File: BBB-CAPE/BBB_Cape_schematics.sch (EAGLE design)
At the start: 84 parts, among them IC1 EEPROM-I2CSMD, SW2 219-02

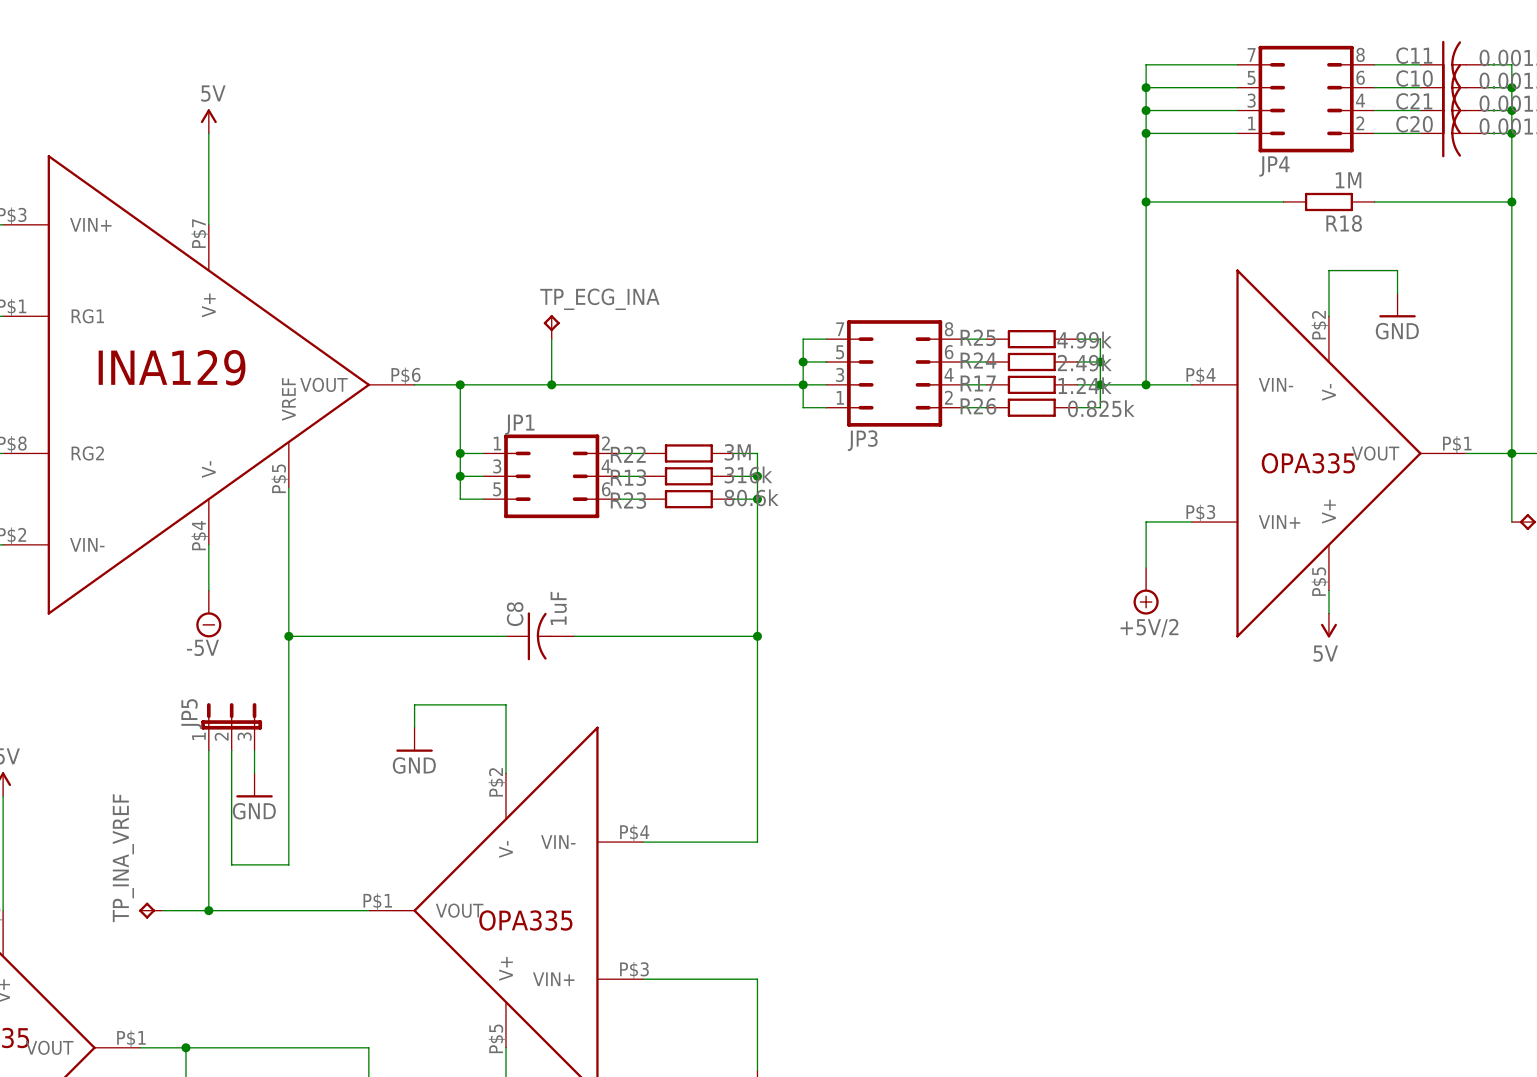
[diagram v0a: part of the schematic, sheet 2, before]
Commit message: Add pin no 1 mark on SOIC-8 and SSOP-8 package in Components.lbr Replace Jumper by Solder jump in BBB_Cape_schematics.sch
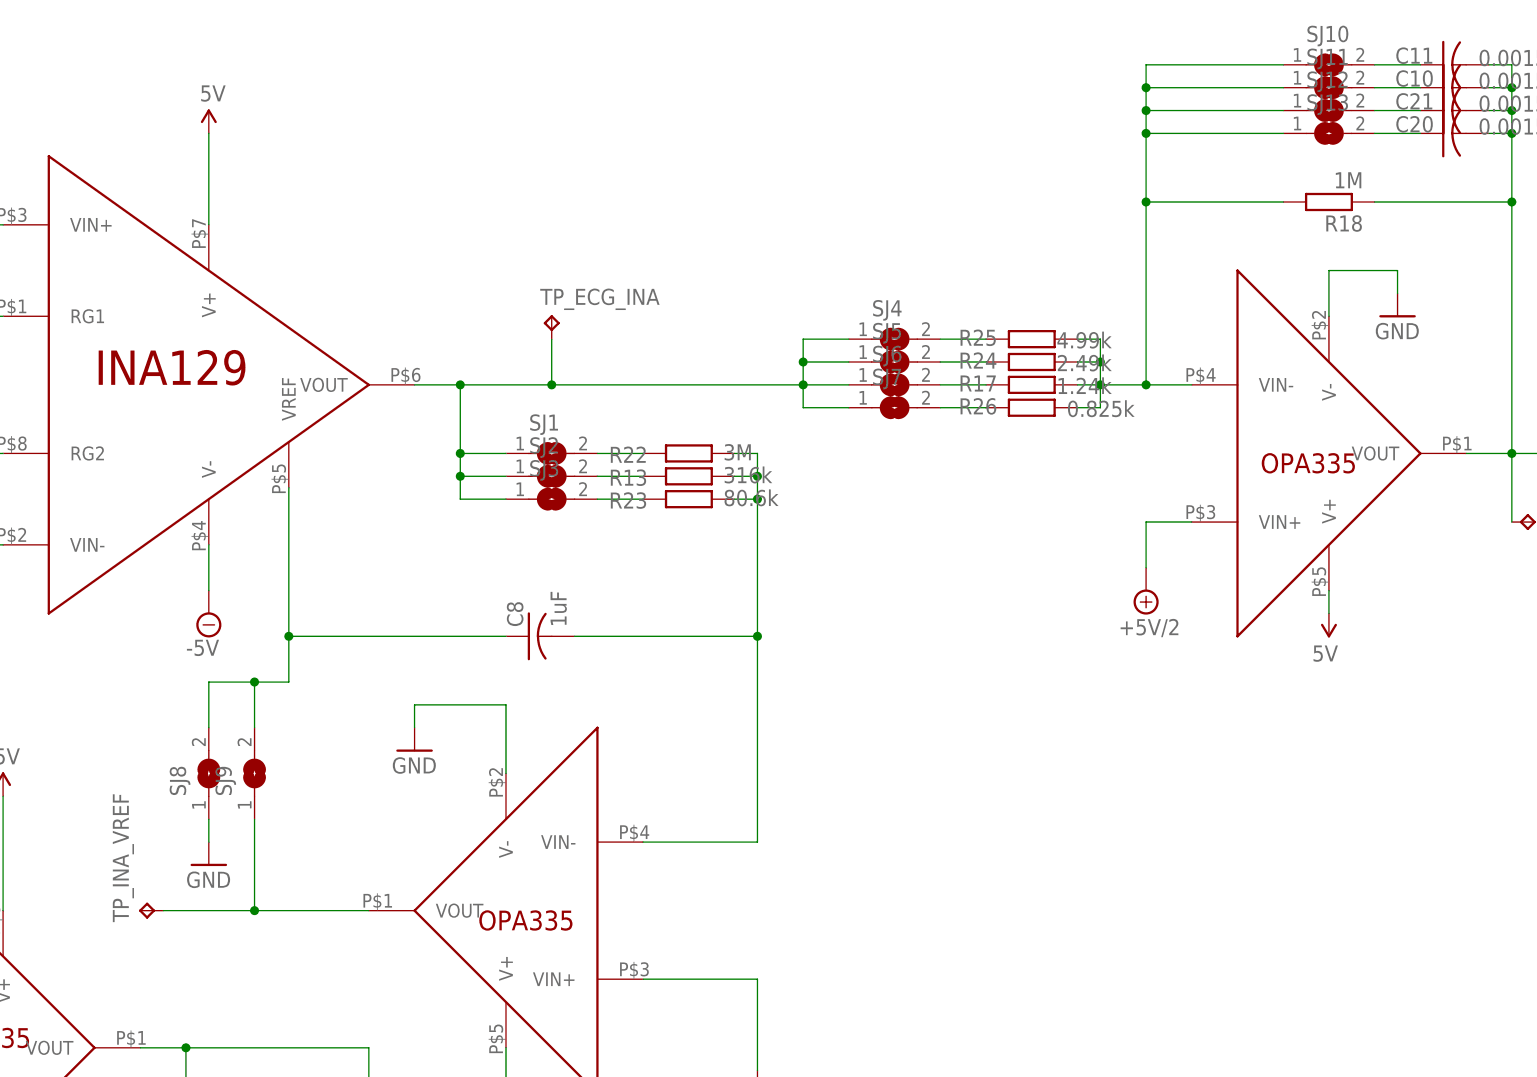
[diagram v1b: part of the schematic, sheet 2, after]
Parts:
- removed JP1: (no value), jumper:JP3Q
- removed JP3, JP4: (no value), jumper:JP4Q
- removed JP5: (no value), jumper:JP2E
- added SJ1, SJ10, SJ11, SJ12, SJ13, SJ2, SJ3, SJ4, SJ5, SJ6, SJ7, SJ8, SJ9: (no value), jumper:SJW
- added TP3, TP4, TP5: TPB2,54, testpad:TPB2,54
- BB1: value BBH2 -> BBH1; device logic-supply:BBH2 -> logic-supply:BBH1
- renumbered U$5 to U5
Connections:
- removed net N$44: C20.1, JP4.2
- new net N$36: R25.2, SJ4.2
- net ADC_DOUT: now also TP3.TP
- net ADC_SCLK: now also TP4.TP
- net GND: now also SJ8.1; no longer JP5.3
- net N$10: now also SJ8.2, SJ9.2; no longer JP5.2
- net N$11: now also SJ1.1, SJ2.1, SJ3.1, SJ4.1, SJ5.1, SJ6.1, SJ7.1; no longer JP1.1, JP1.3, JP1.5, JP3.1, JP3.3, JP3.5, JP3.7
- net N$18: now also SJ10.1, SJ11.1, SJ12.1, SJ13.1; no longer JP4.1, JP4.3, JP4.5, JP4.7
- net N$29: now also TP5.TP
- net N$32: now also SJ1.2; no longer JP1.2
- net N$33: now also SJ2.2; no longer JP1.4
- net N$34: now also SJ3.2; no longer JP1.6
- net N$35: now also SJ9.1; no longer JP5.1
- net N$37: now also R24.2, SJ5.2; no longer JP3.8, R25.2
- net N$38: now also R17.2, SJ6.2; no longer JP3.6, R24.2
- net N$39: now also R26.2, SJ7.2; no longer JP3.4, R17.2
- net N$40: now also C11.1, SJ10.2; no longer JP3.2, R26.2
- net N$41: now also C10.1, SJ11.2; no longer C11.1, JP4.8
- net N$42: now also C21.1, SJ12.2; no longer C10.1, JP4.6
- net N$43: now also C20.1, SJ13.2; no longer C21.1, JP4.4

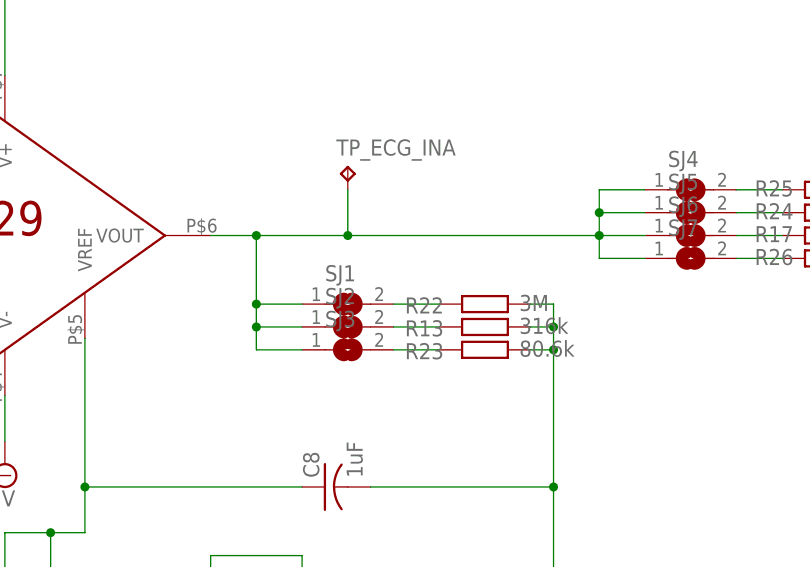
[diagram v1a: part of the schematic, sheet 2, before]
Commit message: Remove one Resistor from LPF in in BBB_Cape_schematics.sch
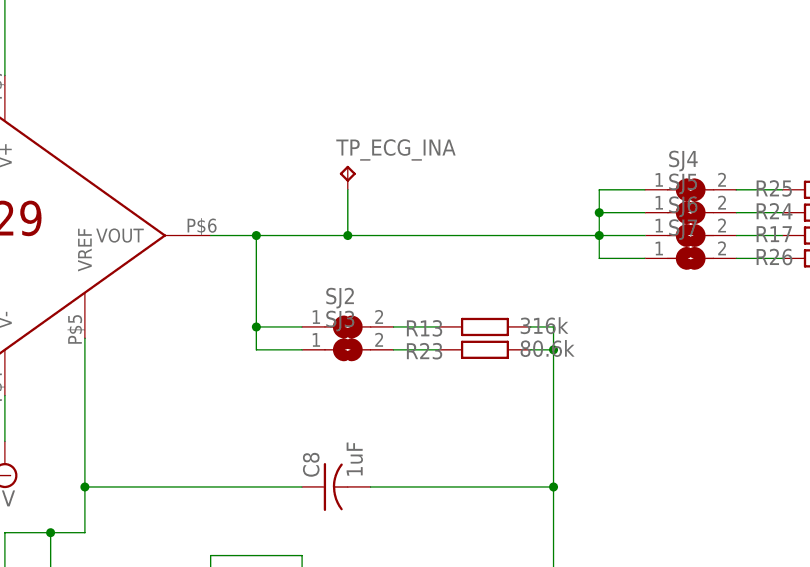
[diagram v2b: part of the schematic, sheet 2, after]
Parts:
- removed R22: 3M, resistor:R-EU_M1206
- removed SJ1: (no value), jumper:SJW
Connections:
- removed net N$32: R22.1, SJ1.2
- net N$11: no longer SJ1.1
- net N$12: no longer R22.2
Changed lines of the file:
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@@
 <part name="R21" library="resistor" deviceset="R-EU_" device="M1206" value="10k"/>
 <part name="P+13" library="SparkFun-Aesthetics" deviceset="3.3V" device=""/>
-<part name="R22" library="resistor" deviceset="R-EU_" device="M1206" value="3M"/>
 <part name="R23" library="resistor" deviceset="R-EU_" device="M1206" value="80.6k"/>
 <part name="GND27" library="supply1" deviceset="GND" device=""/>
@@
 <part name="TP4" library="testpad" deviceset="TP" device="B2,54"/>
 <part name="TP5" library="testpad" deviceset="TP" device="B2,54"/>
-<part name="SJ1" library="jumper" deviceset="SJ" device="W"/>
 <part name="SJ2" library="jumper" deviceset="SJ" device="W"/>
 <part name="SJ3" library="jumper" deviceset="SJ" device="W"/>
@@
 <instance part="TP_ECG_INA" gate="G$1" x="220.98" y="195.58"/>
 <instance part="TP_INA_VREF" gate="G$1" x="175.26" y="129.54" rot="R90"/>
-<instance part="R22" gate="G$1" x="236.22" y="180.34" smashed="yes">
-<attribute name="NAME" x="227.33" y="179.2986" size="1.778" layer="95"/>
-<attribute name="VALUE" x="240.03" y="179.578" size="1.778" layer="96"/>
-</instance>
 <instance part="R23" gate="G$1" x="236.22" y="175.26" smashed="yes">
 <attribute name="NAME" x="227.33" y="174.2186" size="1.778" layer="95"/>
@@
 <instance part="U$31" gate="G$1" x="182.88" y="215.9"/>
 <instance part="U$32" gate="G$1" x="307.34" y="162.56" rot="R180"/>
-<instance part="SJ1" gate="1" x="220.98" y="180.34"/>
 <instance part="SJ2" gate="1" x="220.98" y="177.8"/>
 <instance part="SJ3" gate="1" x="220.98" y="175.26"/>
@@
 <wire x1="210.82" y1="187.96" x2="220.98" y2="187.96" width="0.1524" layer="91"/>
 <wire x1="220.98" y1="193.04" x2="220.98" y2="187.96" width="0.1524" layer="91"/>
-<wire x1="210.82" y1="187.96" x2="210.82" y2="180.34" width="0.1524" layer="91"/>
+<wire x1="210.82" y1="187.96" x2="210.82" y2="177.8" width="0.1524" layer="91"/>
 <junction x="210.82" y="187.96"/>
 <pinref part="SJ3" gate="1" pin="1"/>
-<wire x1="210.82" y1="180.34" x2="210.82" y2="177.8" width="0.1524" layer="91"/>
 <wire x1="210.82" y1="177.8" x2="210.82" y2="175.26" width="0.1524" layer="91"/>
 <wire x1="210.82" y1="175.26" x2="215.9" y2="175.26" width="0.1524" layer="91"/>
@@
 <wire x1="215.9" y1="177.8" x2="210.82" y2="177.8" width="0.1524" layer="91"/>
 <junction x="210.82" y="177.8"/>
-<pinref part="SJ1" gate="1" pin="1"/>
-<wire x1="215.9" y1="180.34" x2="210.82" y2="180.34" width="0.1524" layer="91"/>
-<junction x="210.82" y="180.34"/>
 <wire x1="220.98" y1="187.96" x2="248.92" y2="187.96" width="0.1524" layer="91"/>
 <junction x="220.98" y="187.96"/>
@@
 <pinref part="U$9" gate="G$1" pin="VIN-"/>
 <wire x1="243.84" y1="137.16" x2="231.14" y2="137.16" width="0.1524" layer="91"/>
-<pinref part="R22" gate="G$1" pin="2"/>
-<wire x1="241.3" y1="180.34" x2="243.84" y2="180.34" width="0.1524" layer="91"/>
-<wire x1="243.84" y1="180.34" x2="243.84" y2="177.8" width="0.1524" layer="91"/>
 <junction x="243.84" y="160.02"/>
 <pinref part="R13" gate="G$1" pin="2"/>
@@
 <wire x1="243.84" y1="175.26" x2="243.84" y2="160.02" width="0.1524" layer="91"/>
 <wire x1="241.3" y1="177.8" x2="243.84" y2="177.8" width="0.1524" layer="91"/>
-<junction x="243.84" y="177.8"/>
 <pinref part="R23" gate="G$1" pin="2"/>
 <wire x1="241.3" y1="175.26" x2="243.84" y2="175.26" width="0.1524" layer="91"/>
@@
 </segment>
 </net>
-<net name="N$32" class="0">
-<segment>
-<pinref part="SJ1" gate="1" pin="2"/>
-<pinref part="R22" gate="G$1" pin="1"/>
-<wire x1="226.06" y1="180.34" x2="231.14" y2="180.34" width="0.1524" layer="91"/>
-</segment>
-</net>

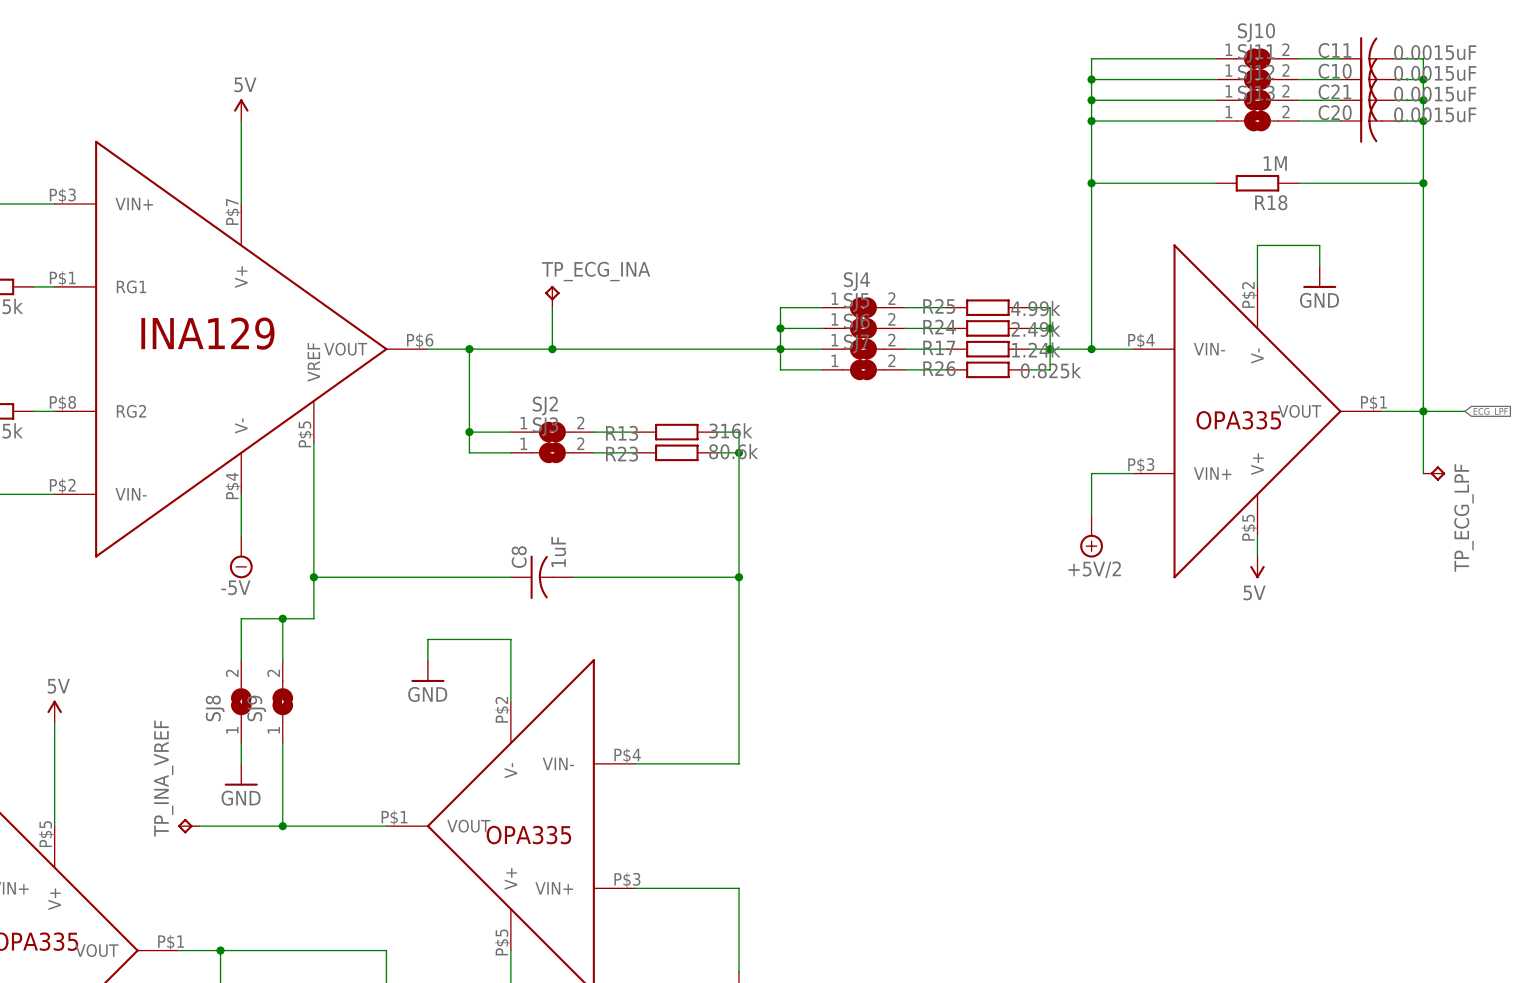
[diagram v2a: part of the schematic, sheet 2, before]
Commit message: Replace solder jump by 0.1 inch header to save space in board in BBB_Cape_schematics.sch
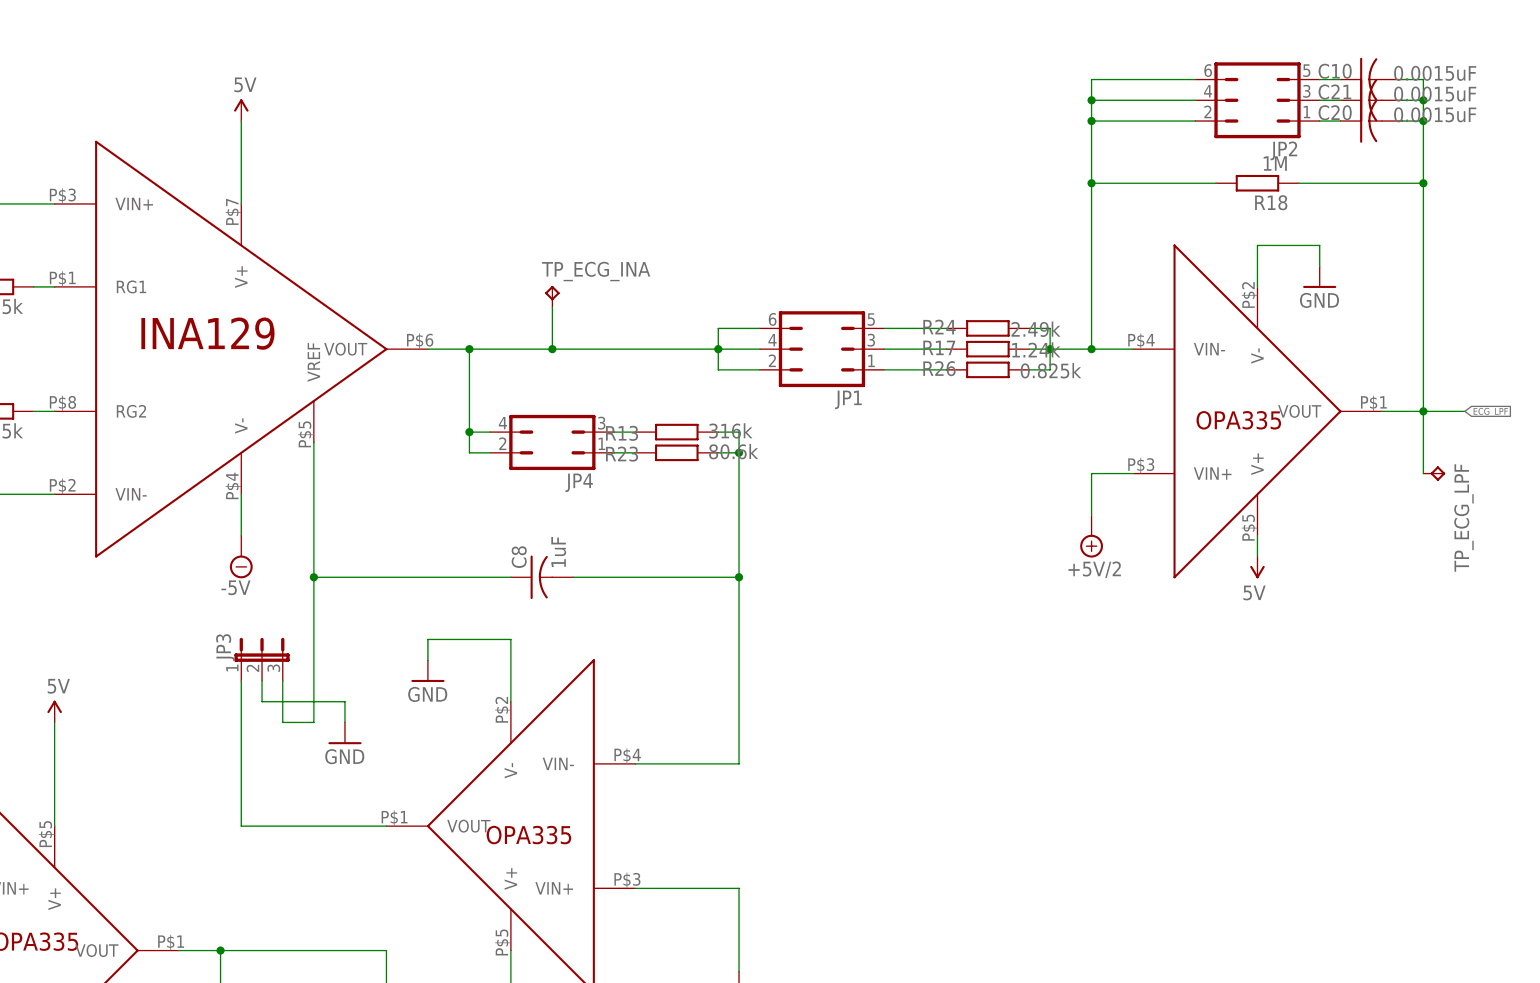
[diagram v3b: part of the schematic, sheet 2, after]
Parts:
- removed C1: 0.1uF, logic-supply:C0402
- removed C11: 0.0015uF, rcl:C-USC1206
- removed IC1: EEPROM-I2CSMD, logic-supply:EEPROM-I2CSMD
- removed R1, R2, R3, R4, R5, R6: 5.6k, logic-supply:R0402
- removed R25: 4.99k, resistor:R-EU_M1206
- removed S2, SW2: 219-02, switch-dil:219-02
- removed SJ10, SJ11, SJ12, SJ13, SJ2, SJ3, SJ4, SJ5, SJ6, SJ7, SJ8, SJ9: (no value), jumper:SJW
- removed TP1, TP2: TEST_POINT, logic-supply:TEST_POINT
- removed TP1_2.5V, TP_INA_VREF: TPB2,54, testpad:TPB2,54
- added JP1, JP2: (no value), jumper:JP3Q
- added JP3: (no value), jumper:JP2E
- added JP4, JP5: (no value), jumper:JP2Q
- renumbered U$10 to U10, U$11 to U11, U$12 to U12, U$13 to U13, U$14 to U14, U$16 to LH, U$17 to RH, U$18 to LH_INDEX, U$19 to U19, U$21 to U21, U$22 to U22, U$23 to U23, U$24 to RH_INDEX, U$4 to U4, U$9 to U9
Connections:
- removed net N$13: IC1.A0, R3.1, SW2.4
- removed net N$14: IC1.A1, R2.1, SW2.3
- removed net N$15: IC1.A2, R1.1
- removed net N$39: R26.2, SJ7.2
- removed net N$43: C20.1, SJ13.2
- removed net WP: IC1.WP, R4.1, TP2.P$1
- net 3.3V: now also JP5.2, JP5.4; no longer C1.1, IC1.VCC, R1.2, R2.2, R3.2, R4.2, R5.2, R6.2, S2.1, S2.2
- net ECG_LPF: no longer C11.2
- net GND: now also JP3.2; no longer C1.2, IC1.VSS, SJ8.1, SW2.1, SW2.2, TP1.P$1
- net I2C2_SCL: no longer IC1.SCL, R5.1
- net I2C2_SDA: no longer IC1.SDA, R6.1
- net N$10: now also JP3.3; no longer SJ8.2, SJ9.2
- net N$11: now also JP1.2, JP1.4, JP1.6, JP4.2, JP4.4; no longer SJ2.1, SJ3.1, SJ4.1, SJ5.1, SJ6.1, SJ7.1
- net N$18: now also JP2.2, JP2.4, JP2.6; no longer R25.1, SJ10.1, SJ11.1, SJ12.1, SJ13.1
- net N$26: no longer TP1_2.5V.TP
- net N$30: now also JP5.3; no longer S2.4
- net N$31: now also JP5.1; no longer S2.3
- net N$33: now also JP4.3; no longer SJ2.2
- net N$34: now also JP4.1; no longer SJ3.2
- net N$35: now also JP3.1; no longer SJ9.1, TP_INA_VREF.TP
- net N$36: now also JP1.5, R24.2; no longer R25.2, SJ4.2
- net N$37: now also JP1.3, R17.2; no longer R24.2, SJ5.2
- net N$38: now also JP1.1, R26.2; no longer R17.2, SJ6.2
- net N$40: now also C10.1, JP2.5; no longer C11.1, SJ10.2
- net N$41: now also C21.1, JP2.3; no longer C10.1, SJ11.2
- net N$42: now also C20.1, JP2.1; no longer C21.1, SJ12.2
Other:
- note removed: "Connect TP1 to GND to disable IC8 write"
- note removed: "EEPROM"
- note removed: "Note:"
- note removed: "protect if reprogramming"
